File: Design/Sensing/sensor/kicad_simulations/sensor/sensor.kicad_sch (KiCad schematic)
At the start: 41 parts, among them J1 Conn_01x14_Pin, J10 Conn_01x02_Pin, J11 Conn_01x01_Pin, J12 Conn_01x02_Pin, J13 Conn_01x02_Pin, J14 Conn_01x02_Pin, J15 Conn_01x02_Pin, J16 Conn_01x01_Pin, J17 Conn_01x02_Pin, J2 Conn_01x14_Pin, J3 Conn_01x02_Pin, J4 Conn_01x02_Pin, J5 Conn_01x02_Pin, J6 Conn_01x01_Pin, J7 Conn_01x02_Pin, J8 Conn_01x02_Pin, J9 Conn_01x02_Pin, Q1 2N3904, Q2 2N3904, Q3 2N3904, U1 TSSP58038, U2 TSSP58038, U3 TSSP58038, U4 BUF602xD, U5 BUF602xD, U6 BUF602xD

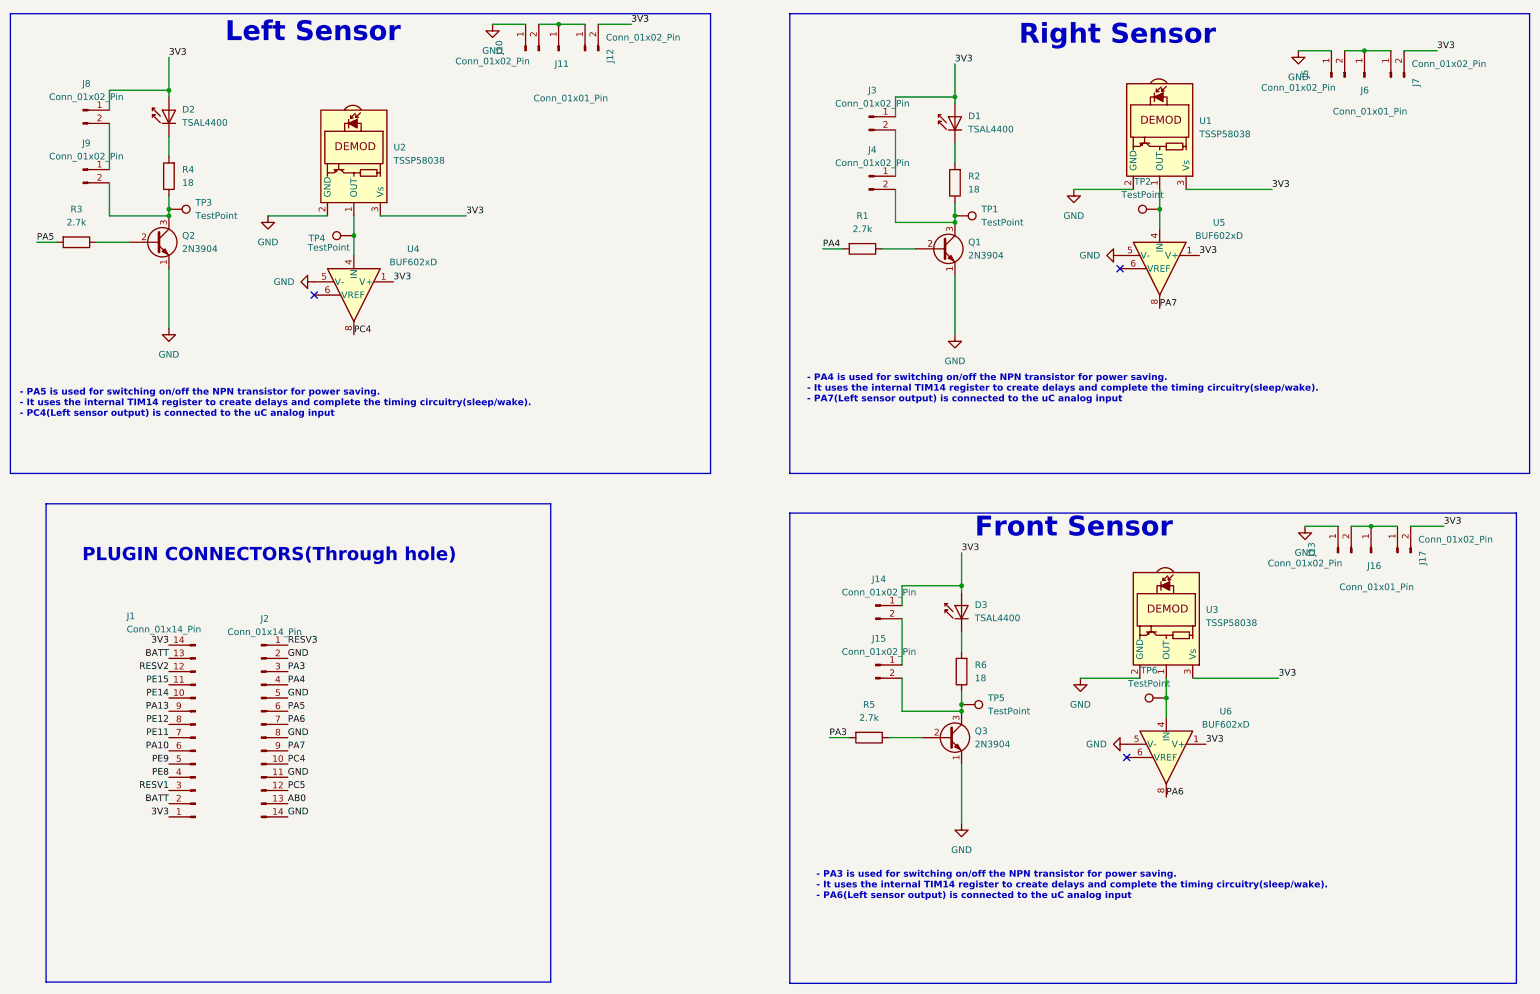
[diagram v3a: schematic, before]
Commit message: PCB components placed but unrooted
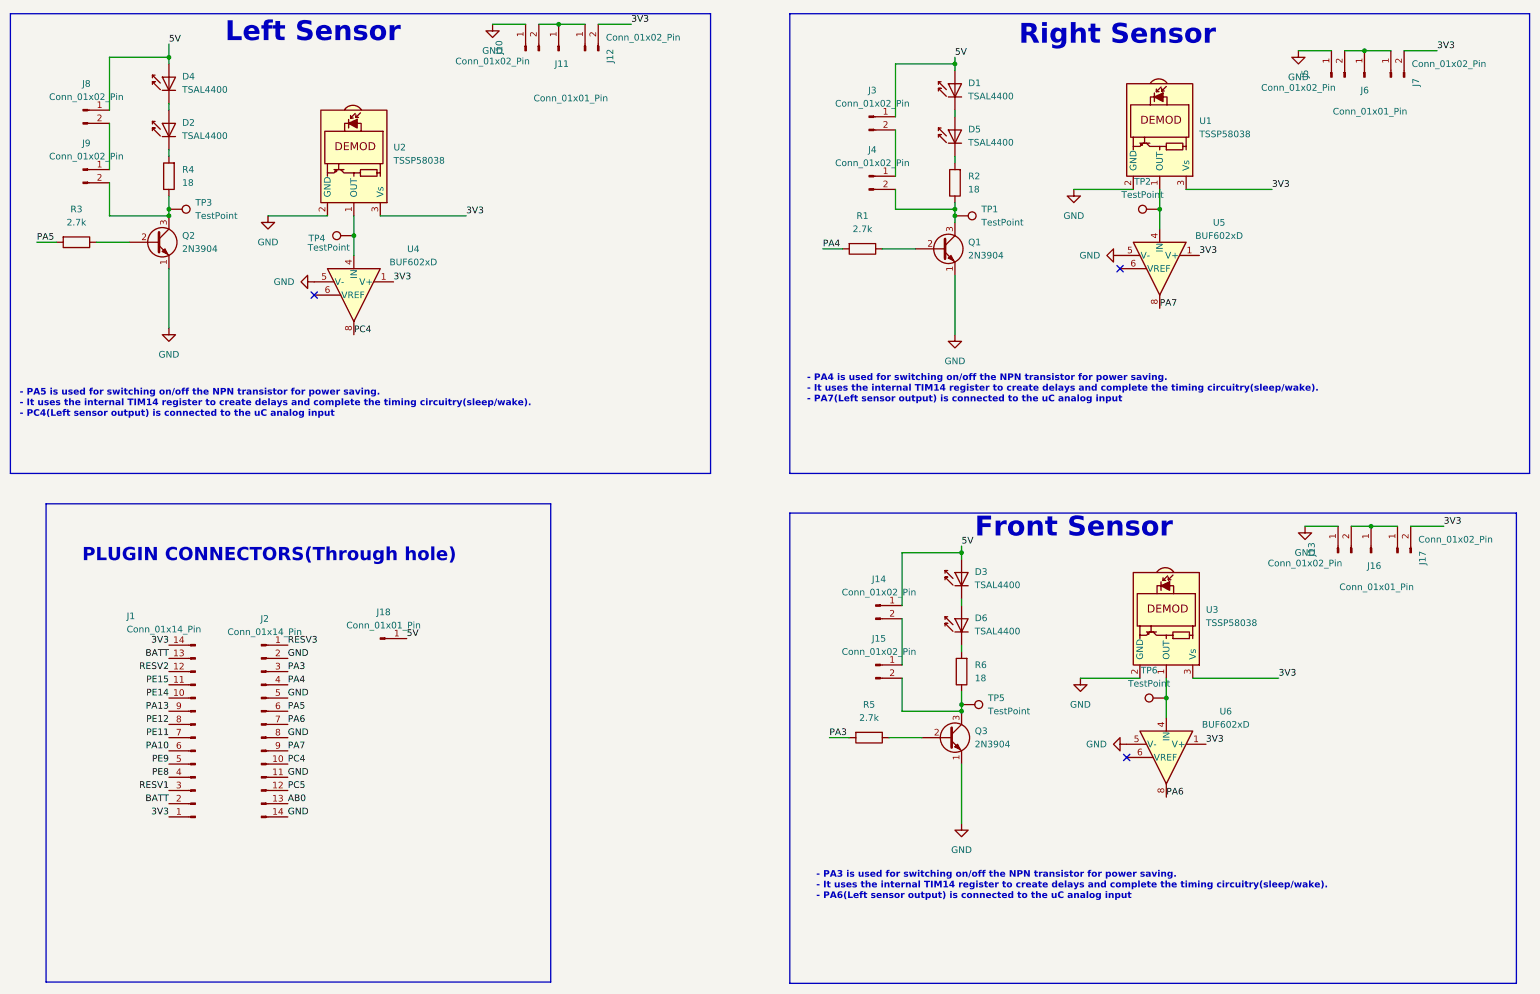
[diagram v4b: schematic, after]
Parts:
- added D4, D5, D6: TSAL4400, LED_THT:LED_D3.0mm_IRBlack, symbol LED:TSAL4400
- added J18: Conn_01x01_Pin, Connector_PinHeader_2.54mm:PinHeader_1x01_P2.54mm_Vertical, symbol Connector:Conn_01x01_Pin
- TP1, TP2, TP3, TP4, TP5, TP6: footprint TestPoint:TestPoint_2Pads_Pitch2.54mm_Drill0.8mm -> TestPoint:TestPoint_Pad_D1.0mm
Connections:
- net 3V3: no longer D1.2 (A), D2.2 (A), D3.2 (A), J14.1 (Pin_1), J3.1 (Pin_1), J8.1 (Pin_1)
- net at D3.1 (K): now also D6.2 (A); no longer R6.2
- net at R2.2: now also D5.1 (K); no longer D1.1 (K)
- new net: D2.2 (A), D4.1 (K)
- new net: D1.1 (K), D5.2 (A)
- new net: D6.1 (K), R6.2
- new net 5V: D1.2 (A), D3.2 (A), D4.2 (A), J14.1 (Pin_1), J18.1 (Pin_1), J3.1 (Pin_1), J8.1 (Pin_1)
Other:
- moved on the sheet: D2
